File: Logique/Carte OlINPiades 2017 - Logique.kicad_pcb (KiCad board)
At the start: 2 copper layers, 100 x 100 mm, 90 parts, among them P1 CONN_01X32, P2 CONN_01X32, P3 CONN_01X02, P4 CONN_01X06, P5 CONN_01X04, P6 CONN_01X02, P7 CONN_FREE_01X03, Q1 MMPQ2907A, Q2 MMPQ2907A, Q3 MMPQ2907A, Q4 MMPQ2907A, Q5 MMPQ2907A, Q6 MMPQ2907A, Q7 MMPQ2907A, Q8 MMPQ2907A, Q9 DSS4160T, U1 74AHC1G, U2 CD74HC154, U3 CD74HC154, U4 STM32F303K8, U5 NCP59301DSS33R4G, Y1 Crystal

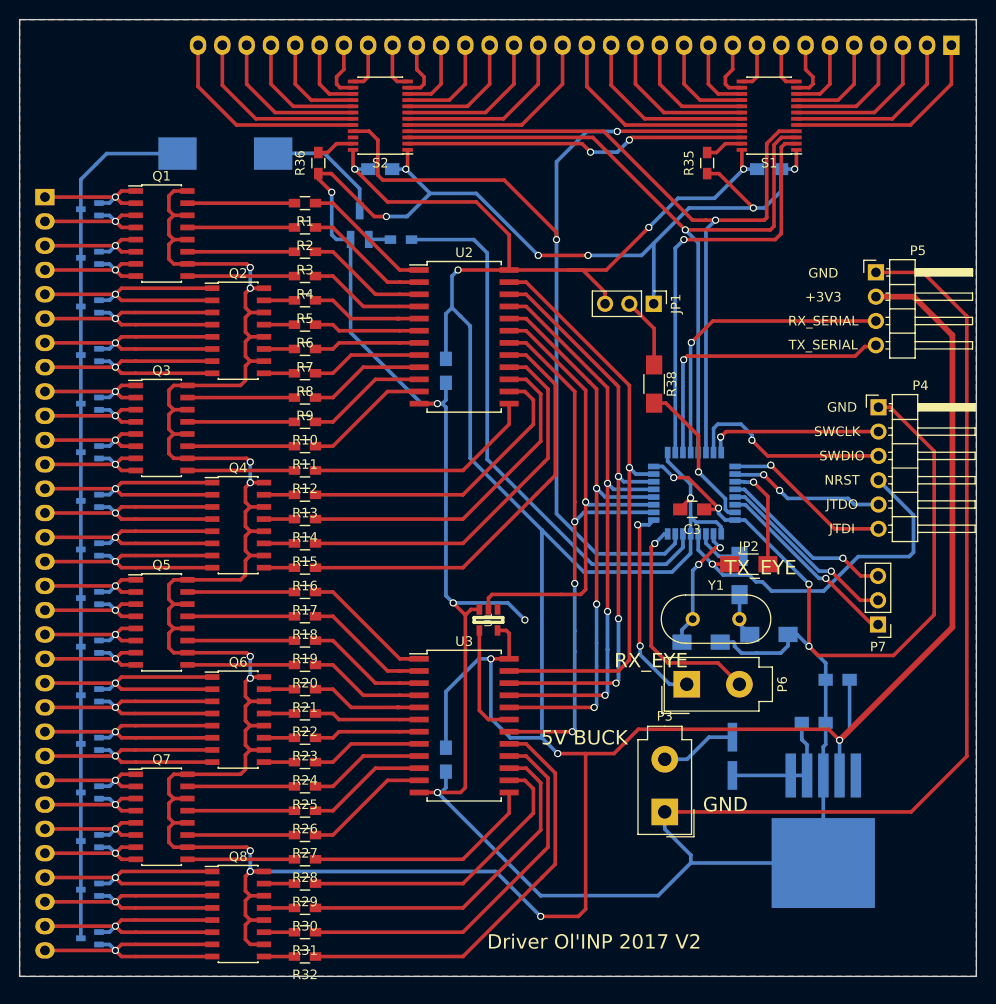
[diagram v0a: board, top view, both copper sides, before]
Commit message: Update schematics and PCB to kicad5
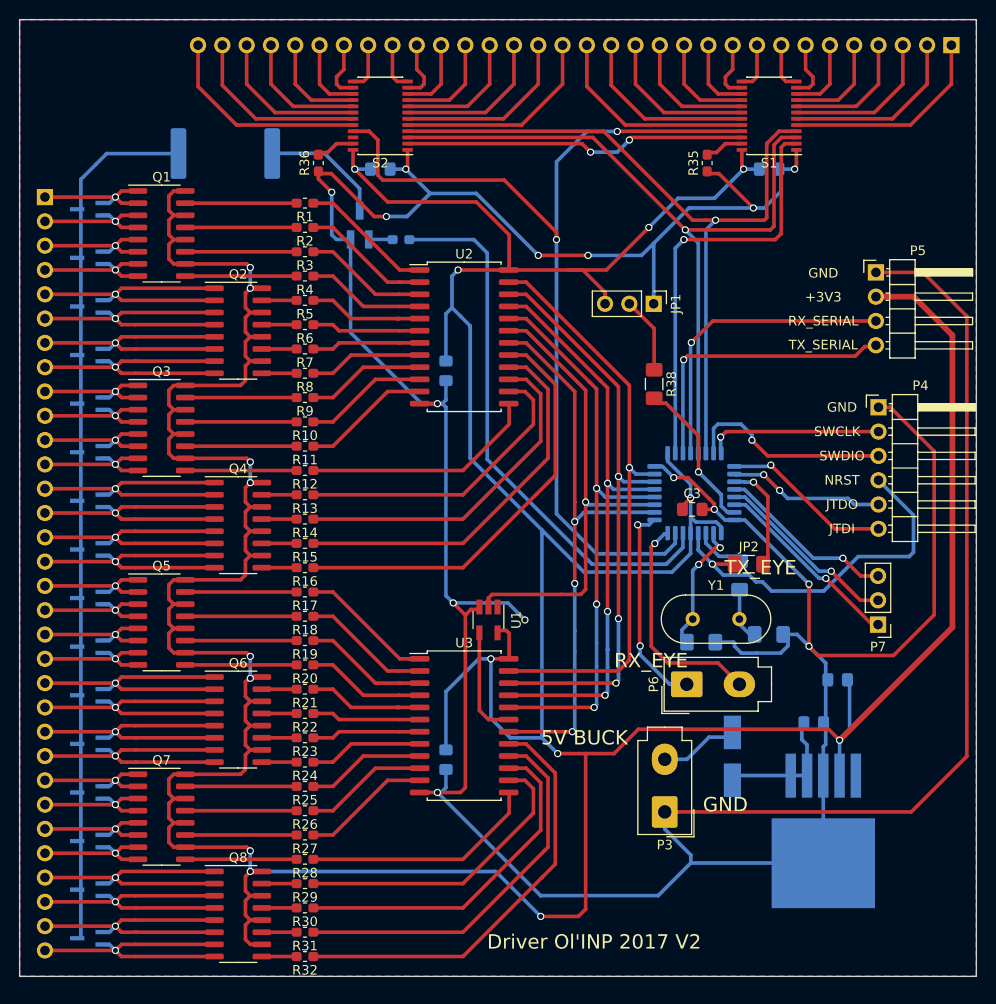
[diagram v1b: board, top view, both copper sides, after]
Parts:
- C1, C2, C3, C4, C5, C7, C8: footprint Capacitors_SMD:C_0805_HandSoldering -> Capacitor_SMD:C_0805_2012Metric_Pad1.15x1.40mm_HandSolder
- C6, C9: footprint Capacitors_SMD:C_1206_HandSoldering -> Capacitor_SMD:C_1206_3216Metric_Pad1.42x1.75mm_HandSolder
- D1, D10, D11, D12, D13, D14, D15, D16, D2, D3, D4, D5, D6, D7, D8, D9: footprint TO_SOT_Packages_SMD:SOT-323 -> Package_TO_SOT_SMD:SOT-323_SC-70_Handsoldering
- D17: footprint Diodes_SMD:SMA_Handsoldering -> Diode_SMD:D_SMA_Handsoldering
- JP1, P7: footprint Pin_Headers:Pin_Header_Straight_1x03_Pitch2.54mm -> Connector_PinHeader_2.54mm:PinHeader_1x03_P2.54mm_Vertical
- JP2, R37, R38: footprint Resistors_SMD:R_1206_HandSoldering -> Resistor_SMD:R_1206_3216Metric_Pad1.42x1.75mm_HandSolder
- P1, P2: footprint Pin_Headers:Pin_Header_Straight_1x32 -> Connector_PinHeader_2.54mm:PinHeader_1x32_P2.54mm_Vertical
- P3, P6: footprint Connectors_Molex_Complete:Molex_MiniFit-JR-5556-02A_2x01x4.20mm_Straight -> Connector_Molex:Molex_Mini-Fit_Jr_5566-02A_2x01_P4.20mm_Vertical
- P4: footprint Pin_Headers:Pin_Header_Angled_1x06_Pitch2.54mm -> Connector_PinHeader_2.54mm:PinHeader_1x06_P2.54mm_Horizontal
- P5: footprint Pin_Headers:Pin_Header_Angled_1x04_Pitch2.54mm -> Connector_PinHeader_2.54mm:PinHeader_1x04_P2.54mm_Horizontal
- Q1, Q2, Q3, Q4, Q5, Q6, Q7, Q8: footprint Housings_SOIC:SOIC-16_3.9x9.9mm_Pitch1.27mm -> Package_SO:SOIC-16_3.9x9.9mm_P1.27mm
- Q9: footprint TO_SOT_Packages_SMD:SOT-23_Handsoldering -> Package_TO_SOT_SMD:SOT-23_Handsoldering
- R1, R10, R11, R12, R13, R14, R15, R16, R17, R18, R19, R2, R20, R21, R22, R23, R24, R25, R26, R27, R28, R29, R3, R30, R31, R32, R34, R35, R36, R4, R5, R6, R7, R8, R9: footprint Resistors_SMD:R_0603_HandSoldering -> Resistor_SMD:R_0603_1608Metric_Pad1.05x0.95mm_HandSolder
- R33: footprint misc:SM_3 -> Resistor_SMD:R_4020_10251Metric_Pad1.65x5.30mm_HandSolder
- S1, S2: footprint Housings_SSOP:TSSOP-24_4.4x7.8mm_Pitch0.65mm -> Package_SO:TSSOP-24_4.4x7.8mm_P0.65mm
- U1: footprint misc:SOT-23-5 -> Package_TO_SOT_SMD:SOT-23-5_HandSoldering
- U2, U3: footprint Housings_SOIC:SOIC-24_7.5x15.4mm_Pitch1.27mm -> Package_SO:SOIC-24W_7.5x15.4mm_P1.27mm
- U4: footprint Housings_QFP:LQFP-32_7x7mm_Pitch0.8mm -> Package_QFP:LQFP-32_7x7mm_P0.8mm
- U5: footprint TO_SOT_Packages_SMD:TO-263-5Lead -> Package_TO_SOT_SMD:TO-263-5_TabPin3
- Y1: footprint Crystals:Crystal_HC49-4H_Vertical -> Crystal:Crystal_HC49-4H_Vertical
- moved U5 5.80 mm to (186.0, 140.8)
- turned C3 to 0 degrees
- turned D1 to 180 degrees
- turned D10 to 180 degrees
- turned D11 to 180 degrees
- turned D12 to 180 degrees
- turned D13 to 180 degrees
- turned D14 to 180 degrees
- turned D15 to 180 degrees
- turned D16 to 180 degrees
- turned D2 to 180 degrees
- turned D3 to 180 degrees
- turned D4 to 180 degrees
- turned D5 to 180 degrees
- turned D6 to 180 degrees
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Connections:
- C3 pad 1: GND -> +3V3
- C3 pad 2: +3V3 -> GND
- S2 pad 22: (no net) -> Net-(S2-Pad22)
- U5 pad 5: (no net) -> Net-(U5-Pad5)
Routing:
- net GND: track 426.2 -> 425.6 mm
